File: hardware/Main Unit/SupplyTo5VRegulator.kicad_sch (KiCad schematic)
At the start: 22 parts, among them U11 TPS56A37RPAR, U12 INA180A3

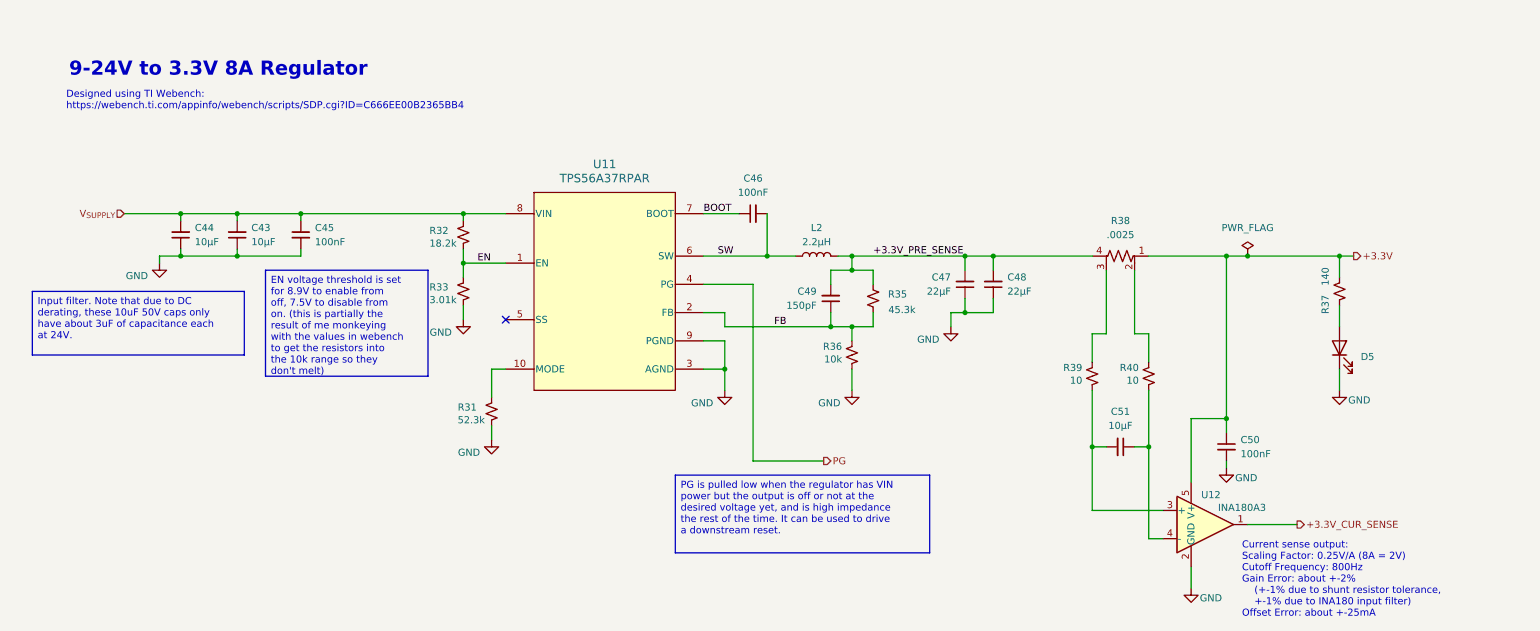
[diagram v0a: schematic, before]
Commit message: Add LEDs and 5V regulator to main unit
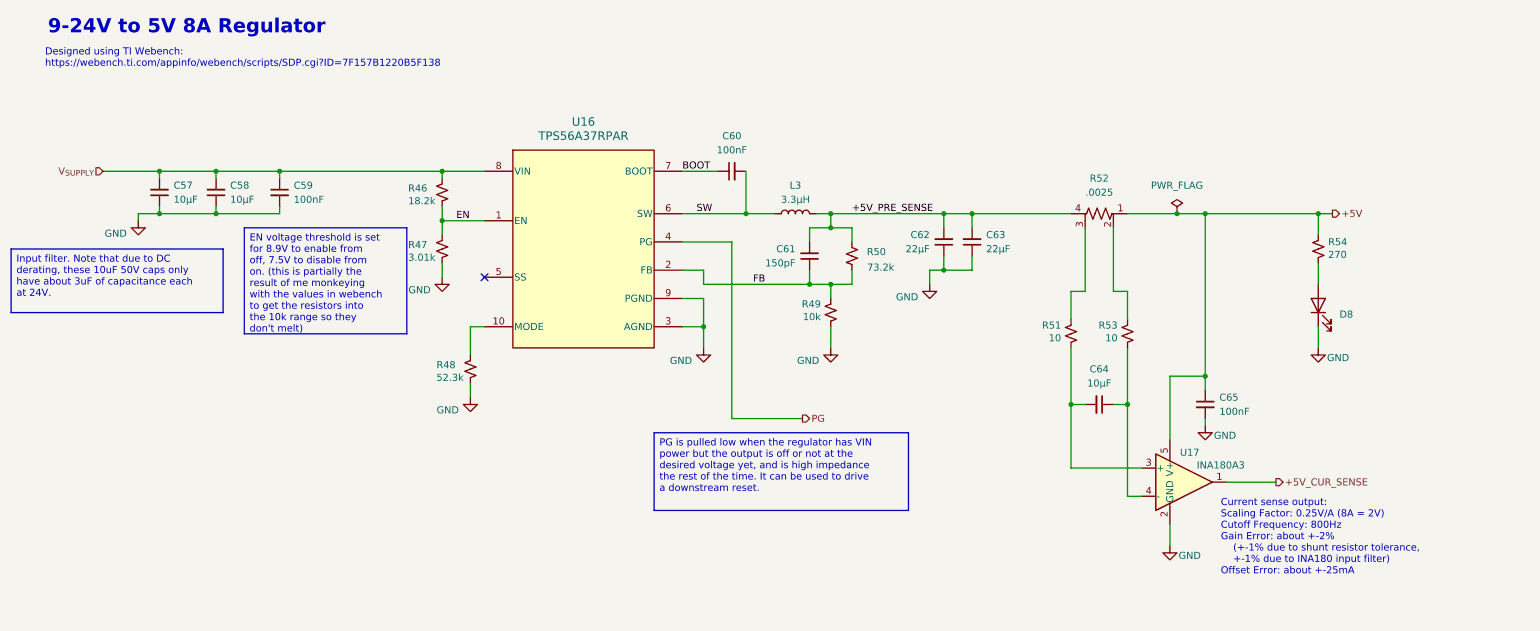
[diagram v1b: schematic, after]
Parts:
- removed C43, C44: 10µF, Capacitor_SMD:C_1210_3225Metric, symbol Device:C_Small
- removed C45, C46, C50: 100nF, Capacitor_SMD:C_0603_1608Metric, symbol Device:C_Small
- removed C47, C48: 22µF, Capacitor_SMD:C_1210_3225Metric, symbol Device:C_Small
- removed C49: 150pF, Capacitor_SMD:C_0603_1608Metric, symbol Device:C_Small
- removed C51: 10µF, Capacitor_SMD:C_1206_3216Metric, symbol Device:C_Small
- removed D5: AA3528CGSK, ColorLEDs:AA3528, symbol ColorLEDs:AA3528CGSK
- removed L2: 2.2μH, Project Library:0630CDMCDDS, symbol Device:L
- removed R31: 52.3k, Resistor_SMD:R_0603_1608Metric, symbol Device:R_Small_US
- removed R32: 18.2k, Resistor_SMD:R_0603_1608Metric, symbol Device:R_Small_US
- removed R33: 3.01k, Resistor_SMD:R_0603_1608Metric, symbol Device:R_Small_US
- removed R35: 45.3k, Resistor_SMD:R_0603_1608Metric, symbol Device:R_Small_US
- removed R36: 10k, Resistor_SMD:R_0603_1608Metric, symbol Device:R_Small_US
- removed R37: 140, Resistor_SMD:R_0603_1608Metric, symbol Device:R_Small_US
- removed R38: .0025, Project Library:D1FCP0612, symbol Device:R_Shunt_US
- removed R39, R40: 10, Resistor_SMD:R_0603_1608Metric, symbol Device:R_Small_US
- removed U11: TPS56A37RPAR, Project Library:RPA0010A-MFG, symbol Project Library:TPS56A37RPAR
- removed U12: INA180A3, Package_TO_SOT_SMD:SOT-23-5, symbol Amplifier_Current:INA180A3
- added C57, C58: 10µF, Capacitor_SMD:C_1210_3225Metric, symbol Device:C_Small
- added C59, C60, C65: 100nF, Capacitor_SMD:C_0603_1608Metric, symbol Device:C_Small
- added C61: 150pF, Capacitor_SMD:C_0603_1608Metric, symbol Device:C_Small
- added C62, C63: 22µF, Capacitor_SMD:C_1210_3225Metric, symbol Device:C_Small
- added C64: 10µF, Capacitor_SMD:C_1206_3216Metric, symbol Device:C_Small
- added D8: AA3528CGSK, ColorLEDs:AA3528, symbol ColorLEDs:AA3528CGSK
- added L3: 3.3μH, Inductor_SMD:L_Vishay_IHLP-3232, symbol Device:L
- added R46: 18.2k, Resistor_SMD:R_0603_1608Metric, symbol Device:R_Small_US
- added R47: 3.01k, Resistor_SMD:R_0603_1608Metric, symbol Device:R_Small_US
- added R48: 52.3k, Resistor_SMD:R_0603_1608Metric, symbol Device:R_Small_US
- added R49: 10k, Resistor_SMD:R_0603_1608Metric, symbol Device:R_Small_US
- added R50: 73.2k, Resistor_SMD:R_0603_1608Metric, symbol Device:R_Small_US
- added R51, R53: 10, Resistor_SMD:R_0603_1608Metric, symbol Device:R_Small_US
- added R52: .0025, Project Library:D1FCP0612, symbol Device:R_Shunt_US
- added R54: 270, Resistor_SMD:R_0603_1608Metric, symbol Device:R_Small_US
- added U16: TPS56A37RPAR, Project Library:RPA0010A-MFG, symbol Project Library:TPS56A37RPAR
- added U17: INA180A3, Package_TO_SOT_SMD:SOT-23-5, symbol Amplifier_Current:INA180A3
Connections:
- net BOOT: now also C60.1, U16.7 (BOOT)
- net EN: now also R46.1, R47.2, U16.1 (EN)
- net FB: now also C61.1, R49.1, R50.1, U16.2 (FB)
- net GND: now also C57.1, C58.1, C59.2, C62.1, C63.1, C65.2, D8.1 (K), R47.1, R48.1, R49.2, U16.3 (AGND), U16.9 (PGND), U17.2 (GND)
- net PG: now also U16.4 (PG)
- net SW: now also C60.2, L3.1, U16.6 (SW)
- net V_{SUPPLY}: now also C57.2, C58.2, C59.1, R46.2, U16.8 (VIN)
- new net: R52.2, R53.1
- new net: R51.1, R52.3
- new net: C64.1, R53.2, U17.4 (-)
- new net: C64.2, R51.2, U17.3 (+)
- new net: D8.2 (A), R54.1
- new net: R48.2, U16.10 (MODE)
- new net +5V: C65.1, R52.1, R54.2, U17.5 (V+)
- new net +5V_CUR_SENSE: U17.1
- new net +5V_PRE_SENSE: C61.2, C62.2, C63.2, L3.2, R50.2, R52.4
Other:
- note added: "9-24V to 5V 8A Regulator"
- note added: "Designed using TI Webench: https://webench.ti.com/appinfo/webench/scripts/SDP.cgi?ID=7F157B1220B5F138"
- note removed: "9-24V to 3.3V 8A Regulator"
- note removed: "Designed using TI Webench: https://webench.ti.com/appinfo/webench/scripts/SDP.cgi?ID=C666EE00B2365BB4"

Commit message: Geographical reannotate
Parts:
- renumbered C63 to C46, C61 to C47, C62 to C51, C64 to C54, C58 to C55, C57 to C56, C65 to C63, C60 to C64, D8 to D7, L3 to L2, R54 to R26, R48 to R30, R50 to R32, R46 to R33, R52 to R35, R49 to R38, R47 to R39, R53 to R46, R51 to R47, U16 to U14
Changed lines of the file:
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@@
 		(on_board yes)
 		(dnp no)
-		(property "Reference" "R50"
+		(property "Reference" "R32"
 			(at 176.276 67.818 0)
 			(effects
@@
 			(project "HackerDAQ Main Unit"
 				(path "/7d91f165-331a-4c48-9d02-ee2a0aa7e94a/567a7564-8dee-43d4-a4d8-4eecc94aa849"
-					(reference "R50")
+					(reference "R32")
 					(unit 1)
 				)
@@
 		(on_board yes)
 		(dnp no)
-		(property "Reference" "R46"
+		(property "Reference" "R33"
 			(at 90.424 56.388 0)
 			(effects
@@
 			(project "HackerDAQ Main Unit"
 				(path "/7d91f165-331a-4c48-9d02-ee2a0aa7e94a/567a7564-8dee-43d4-a4d8-4eecc94aa849"
-					(reference "R46")
+					(reference "R33")
 					(unit 1)
 				)
@@
 		(dnp no)
 		(fields_autoplaced yes)
-		(property "Reference" "C57"
+		(property "Reference" "C56"
 			(at 48.26 55.8736 0)
 			(effects
@@
 			(project "HackerDAQ Main Unit"
 				(path "/7d91f165-331a-4c48-9d02-ee2a0aa7e94a/567a7564-8dee-43d4-a4d8-4eecc94aa849"
-					(reference "C57")
+					(reference "C56")
 					(unit 1)
 				)
@@
 		(on_board yes)
 		(dnp no)
-		(property "Reference" "C61"
+		(property "Reference" "C47"
 			(at 160.02 67.3035 0)
 			(effects
@@
 			(project "HackerDAQ Main Unit"
 				(path "/7d91f165-331a-4c48-9d02-ee2a0aa7e94a/567a7564-8dee-43d4-a4d8-4eecc94aa849"
-					(reference "C61")
+					(reference "C47")
 					(unit 1)
 				)
@@
 		(dnp no)
 		(fields_autoplaced yes)
-		(property "Reference" "R52"
+		(property "Reference" "R35"
 			(at 214.63 54.61 90)
 			(effects
@@
 			(project "HackerDAQ Main Unit"
 				(path "/7d91f165-331a-4c48-9d02-ee2a0aa7e94a/567a7564-8dee-43d4-a4d8-4eecc94aa849"
-					(reference "R52")
+					(reference "R35")
 					(unit 1)
 				)
@@
 		(dnp no)
 		(fields_autoplaced yes)
-		(property "Reference" "C58"
+		(property "Reference" "C55"
 			(at 58.42 55.8736 0)
 			(effects
@@
 			(project "HackerDAQ Main Unit"
 				(path "/7d91f165-331a-4c48-9d02-ee2a0aa7e94a/567a7564-8dee-43d4-a4d8-4eecc94aa849"
-					(reference "C58")
+					(reference "C55")
 					(unit 1)
 				)
@@
 		(dnp no)
 		(fields_autoplaced yes)
-		(property "Reference" "C64"
+		(property "Reference" "C54"
 			(at 214.6236 88.9 90)
 			(effects
@@
 			(project "HackerDAQ Main Unit"
 				(path "/7d91f165-331a-4c48-9d02-ee2a0aa7e94a/567a7564-8dee-43d4-a4d8-4eecc94aa849"
-					(reference "C64")
+					(reference "C54")
 					(unit 1)
 				)
@@
 		(on_board yes)
 		(dnp no)
-		(property "Reference" "R54"
+		(property "Reference" "R26"
 			(at 255.778 66.04 0)
 			(effects
@@
 			(project "HackerDAQ Main Unit"
 				(path "/7d91f165-331a-4c48-9d02-ee2a0aa7e94a/567a7564-8dee-43d4-a4d8-4eecc94aa849"
-					(reference "R54")
+					(reference "R26")
 					(unit 1)
 				)
@@
 		(on_board yes)
 		(dnp no)
-		(property "Reference" "C62"
+		(property "Reference" "C51"
 			(at 184.15 64.7636 0)
 			(effects
@@
 			(project "HackerDAQ Main Unit"
 				(path "/7d91f165-331a-4c48-9d02-ee2a0aa7e94a/567a7564-8dee-43d4-a4d8-4eecc94aa849"
-					(reference "C62")
+					(reference "C51")
 					(unit 1)
 				)
@@
 		(dnp no)
 		(fields_autoplaced yes)
-		(property "Reference" "C63"
+		(property "Reference" "C46"
 			(at 194.31 64.7636 0)
 			(effects
@@
 			(project "HackerDAQ Main Unit"
 				(path "/7d91f165-331a-4c48-9d02-ee2a0aa7e94a/567a7564-8dee-43d4-a4d8-4eecc94aa849"
-					(reference "C63")
+					(reference "C46")
 					(unit 1)
 				)
@@
 		(on_board yes)
 		(dnp no)
-		(property "Reference" "R48"
+		(property "Reference" "R30"
 			(at 95.504 88.138 0)
 			(effects
@@
 			(project "HackerDAQ Main Unit"
 				(path "/7d91f165-331a-4c48-9d02-ee2a0aa7e94a/567a7564-8dee-43d4-a4d8-4eecc94aa849"
-					(reference "R48")
+					(reference "R30")
 					(unit 1)
 				)
@@
 		(on_board yes)
 		(dnp no)
-		(property "Reference" "R53"
+		(property "Reference" "R46"
 			(at 217.932 81.026 0)
 			(effects
@@
 			(project "HackerDAQ Main Unit"
 				(path "/7d91f165-331a-4c48-9d02-ee2a0aa7e94a/567a7564-8dee-43d4-a4d8-4eecc94aa849"
-					(reference "R53")
+					(reference "R46")
 					(unit 1)
 				)
@@
 		(on_board yes)
 		(dnp no)
-		(property "Reference" "R51"
+		(property "Reference" "R47"
 			(at 207.772 81.026 0)
 			(effects
@@
 			(project "HackerDAQ Main Unit"
 				(path "/7d91f165-331a-4c48-9d02-ee2a0aa7e94a/567a7564-8dee-43d4-a4d8-4eecc94aa849"
-					(reference "R51")
+					(reference "R47")
 					(unit 1)
 				)
@@
 		(dnp no)
 		(fields_autoplaced yes)
-		(property "Reference" "C60"
+		(property "Reference" "C64"
 			(at 148.5963 46.99 90)
 			(effects
@@
 			(project "HackerDAQ Main Unit"
 				(path "/7d91f165-331a-4c48-9d02-ee2a0aa7e94a/567a7564-8dee-43d4-a4d8-4eecc94aa849"
-					(reference "C60")
+					(reference "C64")
 					(unit 1)
 				)
@@
 		(dnp no)
 		(fields_autoplaced yes)
-		(property "Reference" "D8"
+		(property "Reference" "D7"
 			(at 257.81 79.0574 90)
 			(effects
@@
 			(project "HackerDAQ Main Unit"
 				(path "/7d91f165-331a-4c48-9d02-ee2a0aa7e94a/567a7564-8dee-43d4-a4d8-4eecc94aa849"
-					(reference "D8")
+					(reference "D7")
 					(unit 1)
 				)
@@
 		(on_board yes)
 		(dnp no)
-		(property "Reference" "R49"
+		(property "Reference" "R38"
 			(at 164.592 77.216 0)
 			(effects
@@
 			(project "HackerDAQ Main Unit"
 				(path "/7d91f165-331a-4c48-9d02-ee2a0aa7e94a/567a7564-8dee-43d4-a4d8-4eecc94aa849"
-					(reference "R49")
+					(reference "R38")
 					(unit 1)
 				)
@@
 		(dnp no)
 		(fields_autoplaced yes)
-		(property "Reference" "L3"
+		(property "Reference" "L2"
 			(at 160.02 55.88 90)
 			(effects
@@
 			(project "HackerDAQ Main Unit"
 				(path "/7d91f165-331a-4c48-9d02-ee2a0aa7e94a/567a7564-8dee-43d4-a4d8-4eecc94aa849"
-					(reference "L3")
+					(reference "L2")
 					(unit 1)
 				)
@@
 		(dnp no)
 		(fields_autoplaced yes)
-		(property "Reference" "C65"
+		(property "Reference" "C63"
 			(at 236.22 93.9862 0)
 			(effects
@@
 			(project "HackerDAQ Main Unit"
 				(path "/7d91f165-331a-4c48-9d02-ee2a0aa7e94a/567a7564-8dee-43d4-a4d8-4eecc94aa849"
-					(reference "C65")
+					(reference "C63")
 					(unit 1)
 				)
@@
 		(dnp no)
 		(fields_autoplaced yes)
-		(property "Reference" "U16"
+		(property "Reference" "U14"
 			(at 121.92 44.45 0)
 			(effects
@@
 			(project "HackerDAQ Main Unit"
 				(path "/7d91f165-331a-4c48-9d02-ee2a0aa7e94a/567a7564-8dee-43d4-a4d8-4eecc94aa849"
-					(reference "U16")
+					(reference "U14")
 					(unit 1)
 				)
@@
 		(on_board yes)
 		(dnp no)
-		(property "Reference" "R47"
+		(property "Reference" "R39"
 			(at 90.424 66.548 0)
 			(effects
@@
 			(project "HackerDAQ Main Unit"
 				(path "/7d91f165-331a-4c48-9d02-ee2a0aa7e94a/567a7564-8dee-43d4-a4d8-4eecc94aa849"
-					(reference "R47")
-					(unit 1)
-				)
+					(reference "R39")
+					(unit 1)
+				)
